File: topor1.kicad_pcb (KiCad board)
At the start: 2 copper layers, 99.8 x 99.8 mm, 76 parts, among them IC1 ATMEGA168-A, P1 CONN_01X02_PWR, P2 USB_B, P3 CONN_02X13_X0, P4 CONN_02X13_X3, P5 CONN_02X13_X1, P6 CONN_02X07_JTAG, U1 AP1117_ADJ, U2 AP1117_33, U3 AP1117_ADJ, U4 FT232RL, U5 M25P16-VME, U6 ECS-3963, U7 XC6SLX9-TQG144, Y1 11.059MHz

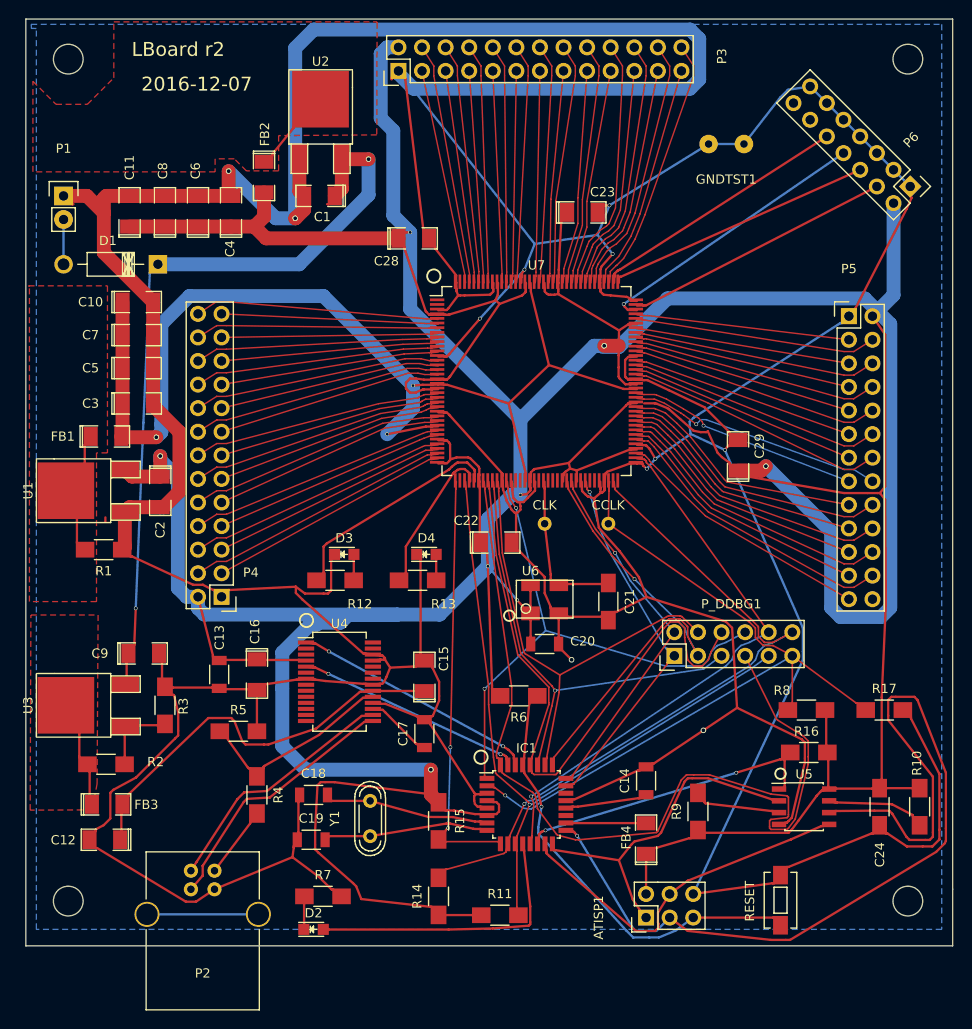
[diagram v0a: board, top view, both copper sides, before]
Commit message: Spartan-6 chip position was changed to avoid problems with a bent tracks. CD6 net was rerouted.
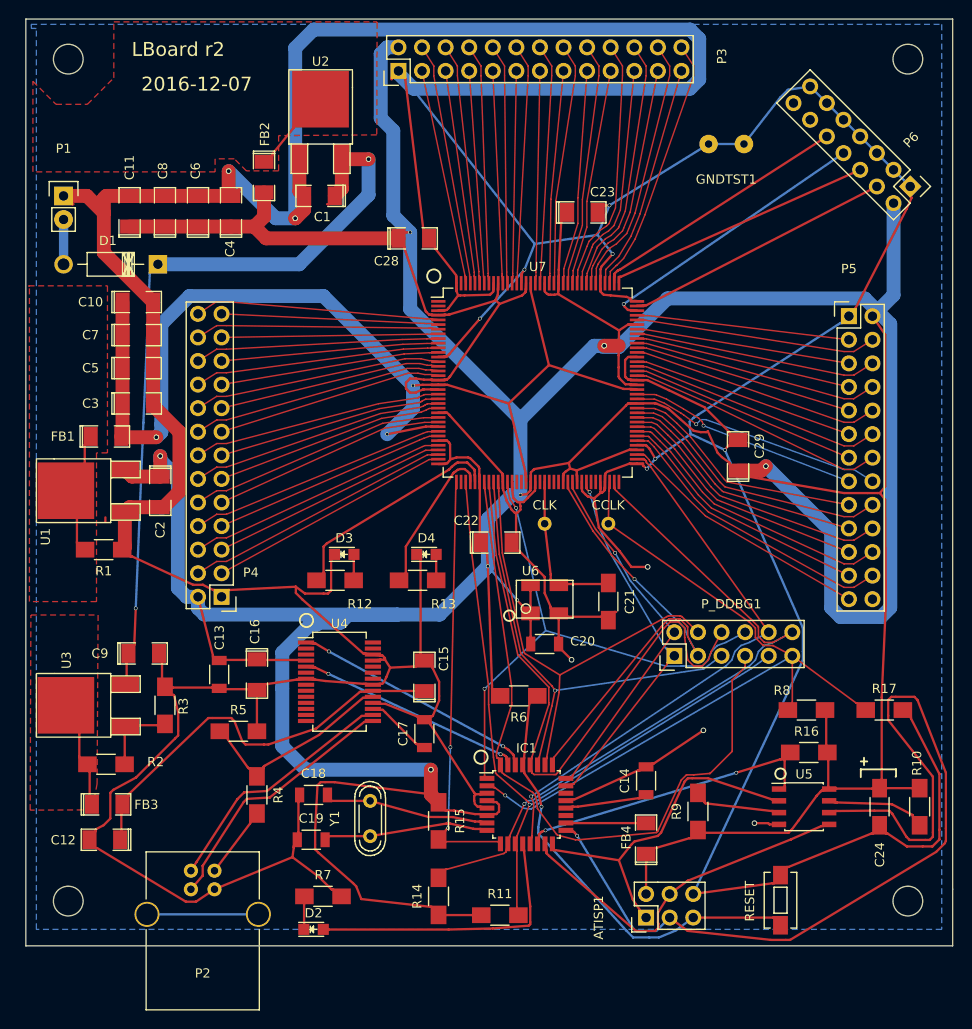
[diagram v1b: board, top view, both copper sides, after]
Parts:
- moved U7 0.21 mm to (120.2, 102.2)
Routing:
- net GND: track 836.7 -> 793.6 mm, vias 11 -> 13
- net /mcu/CD6: track 99.3 -> 76.0 mm

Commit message: bumped revision number, made some minort track layout changes
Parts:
- moved U7 0.05 mm to (120.2, 102.1)
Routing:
- net GND: track 793.6 -> 794.8 mm
- net /mcu/CD0: track 39.8 -> 40.6 mm
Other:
- board text added: "2016-12-20"
- board text added: "LBoard r3"
- board text removed: "2016-12-07"
- board text removed: "LBoard r2"

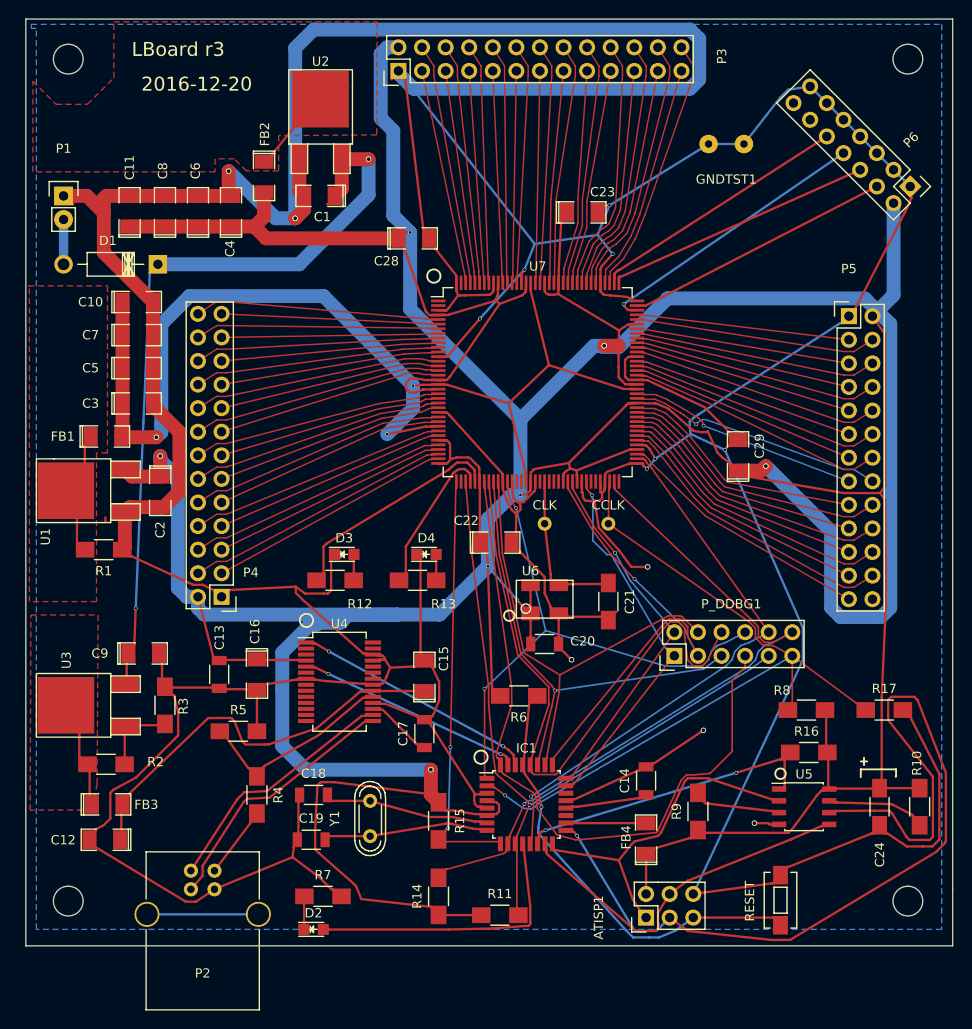
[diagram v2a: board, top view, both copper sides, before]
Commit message: footprint of oscillator Y1 changed. Some silscreen changes
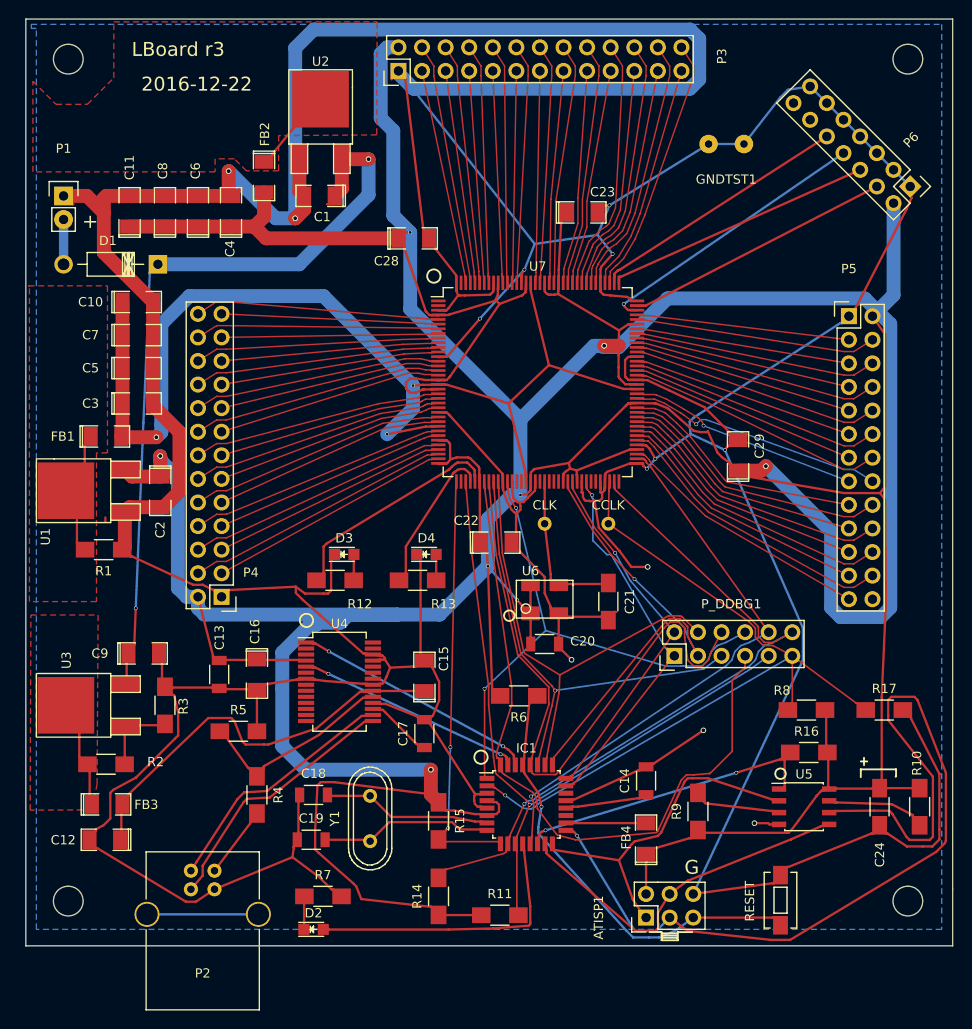
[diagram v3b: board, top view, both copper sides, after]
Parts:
- Y1: footprint Crystals:Crystal_HC52-U_Vertical -> Crystals:Crystal_HC49-U_Vertical
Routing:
- net Net-(C19-Pad2): track 17.8 -> 20.2 mm
- net Net-(C18-Pad2): track 17.8 -> 19.1 mm
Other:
- board text added: "+"
- board text added: "2016-12-22"
- board text added: "G"
- board text removed: "2016-12-20"

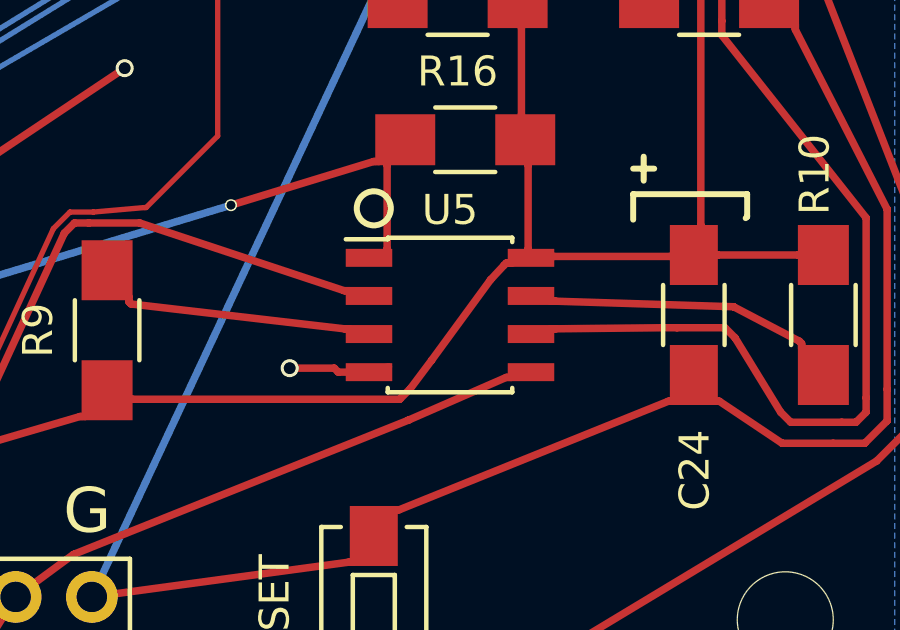
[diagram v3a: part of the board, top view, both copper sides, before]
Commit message: New footprint for SOIC-8W.
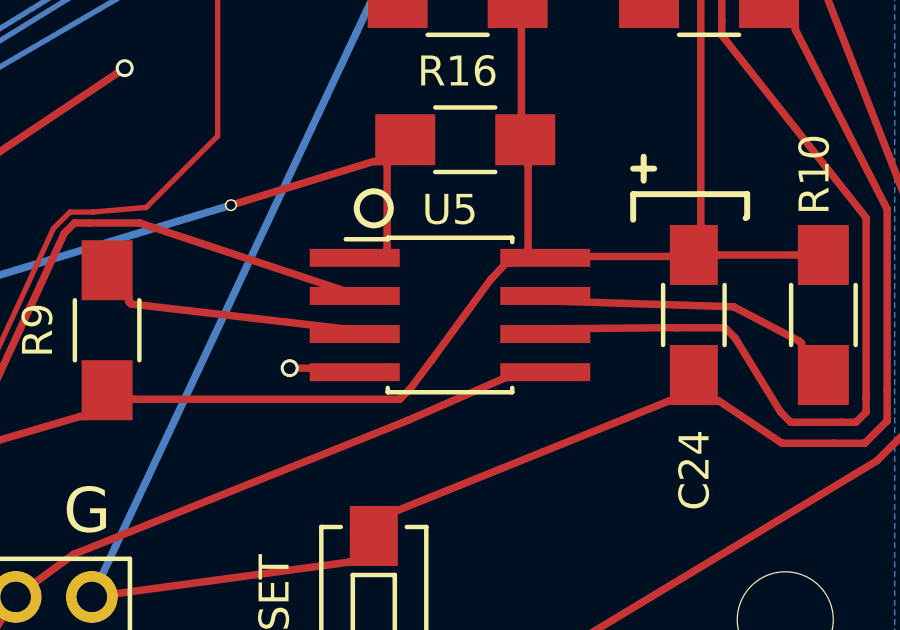
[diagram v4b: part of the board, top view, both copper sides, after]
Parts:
- U5: footprint Housings_SOIC:SOIC-8_3.9x4.9mm_Pitch1.27mm -> SOIC-8W-LONGPAD:SOIC-8_5.49x5.49mm_Pitch1.27mm
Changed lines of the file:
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@@
-    )
-  )
-  (module Housings_SOIC:SOIC-8_3.9x4.9mm_Pitch1.27mm (layer F.Cu)
-    (at 148.844 147.828)
-    (descr "8-Lead Plastic Small Outline (SN) - Narrow, 3.90 mm Body [SOIC] (see Microchip Packaging Specification 00000049BS.pdf)")
-    (tags "SOIC 1.27")
-    (attr smd)
-    (fp_text reference U5 (at 0 -3.5) (layer F.SilkS)
-      (effects (font (size 1 1) (thickness 0.15)))
-    )
-    (fp_text value M25P16-VME (at 0 3.5) (layer F.Fab)
-      (effects (font (size 1 1) (thickness 0.15)))
-    )
-    (fp_line (start -0.95 -2.45) (end 1.95 -2.45) (layer F.Fab) (width 0.15))
-    (fp_line (start 1.95 -2.45) (end 1.95 2.45) (layer F.Fab) (width 0.15))
-    (fp_line (start 1.95 2.45) (end -1.95 2.45) (layer F.Fab) (width 0.15))
-    (fp_line (start -1.95 2.45) (end -1.95 -1.45) (layer F.Fab) (width 0.15))
-    (fp_line (start -1.95 -1.45) (end -0.95 -2.45) (layer F.Fab) (width 0.15))
-    (fp_line (start -3.75 -2.75) (end -3.75 2.75) (layer F.CrtYd) (width 0.05))
-    (fp_line (start 3.75 -2.75) (end 3.75 2.75) (layer F.CrtYd) (width 0.05))
-    (fp_line (start -3.75 -2.75) (end 3.75 -2.75) (layer F.CrtYd) (width 0.05))
-    (fp_line (start -3.75 2.75) (end 3.75 2.75) (layer F.CrtYd) (width 0.05))
-    (fp_line (start -2.075 -2.575) (end -2.075 -2.525) (layer F.SilkS) (width 0.15))
-    (fp_line (start 2.075 -2.575) (end 2.075 -2.43) (layer F.SilkS) (width 0.15))
-    (fp_line (start 2.075 2.575) (end 2.075 2.43) (layer F.SilkS) (width 0.15))
-    (fp_line (start -2.075 2.575) (end -2.075 2.43) (layer F.SilkS) (width 0.15))
-    (fp_line (start -2.075 -2.575) (end 2.075 -2.575) (layer F.SilkS) (width 0.15))
-    (fp_line (start -2.075 2.575) (end 2.075 2.575) (layer F.SilkS) (width 0.15))
-    (fp_line (start -2.075 -2.525) (end -3.475 -2.525) (layer F.SilkS) (width 0.15))
-    (pad 1 smd rect (at -2.7 -1.905) (size 1.55 0.6) (layers F.Cu F.Paste F.Mask)
-      (net 30 "Net-(IC1-Pad14)"))
-    (pad 2 smd rect (at -2.7 -0.635) (size 1.55 0.6) (layers F.Cu F.Paste F.Mask)
-      (net 1 /mcu/MISO))
-    (pad 3 smd rect (at -2.7 0.635) (size 1.55 0.6) (layers F.Cu F.Paste F.Mask)
-      (net 126 "Net-(R9-Pad2)"))
-    (pad 4 smd rect (at -2.7 1.905) (size 1.55 0.6) (layers F.Cu F.Paste F.Mask)
-      (net 6 GND))
-    (pad 5 smd rect (at 2.7 1.905) (size 1.55 0.6) (layers F.Cu F.Paste F.Mask)
-      (net 4 /mcu/MOSI))
-    (pad 6 smd rect (at 2.7 0.635) (size 1.55 0.6) (layers F.Cu F.Paste F.Mask)
-      (net 3 "Net-(ATISP1-Pad3)"))
-    (pad 7 smd rect (at 2.7 -0.635) (size 1.55 0.6) (layers F.Cu F.Paste F.Mask)
-      (net 127 "Net-(R10-Pad2)"))
-    (pad 8 smd rect (at 2.7 -1.905) (size 1.55 0.6) (layers F.Cu F.Paste F.Mask)
-      (net 2 +3V3))
-    (model Housings_SOIC.3dshapes/SOIC-8_3.9x4.9mm_Pitch1.27mm.wrl
-      (at (xyz 0 0 0))
-      (scale (xyz 1 1 1))
-      (rotate (xyz 0 0 0))
     )
   )
@@
       (net 12 "Net-(C18-Pad2)"))
   )
+  (module SOIC-8W-LONGPAD:SOIC-8_5.49x5.49mm_Pitch1.27mm (layer F.Cu)
+    (at 148.844 147.828)
+    (tags "SOIC 1.27")
+    (attr smd)
+    (fp_text reference U5 (at 0 -3.5) (layer F.SilkS)
+      (effects (font (size 1 1) (thickness 0.15)))
+    )
+    (fp_text value M25P16-VME (at 0 3.5) (layer F.Fab)
+      (effects (font (size 1 1) (thickness 0.15)))
+    )
+    (fp_line (start -0.95 -2.45) (end 1.95 -2.45) (layer F.Fab) (width 0.15))
+    (fp_line (start 1.95 -2.45) (end 1.95 2.45) (layer F.Fab) (width 0.15))
+    (fp_line (start 1.95 2.45) (end -1.95 2.45) (layer F.Fab) (width 0.15))
+    (fp_line (start -1.95 2.45) (end -1.95 -1.45) (layer F.Fab) (width 0.15))
+    (fp_line (start -1.95 -1.45) (end -0.95 -2.45) (layer F.Fab) (width 0.15))
+    (fp_line (start -4.953 -2.7305) (end -4.953 2.7695) (layer F.CrtYd) (width 0.05))
+    (fp_line (start 4.953 -2.7305) (end 4.953 2.7695) (layer F.CrtYd) (width 0.05))
+    (fp_line (start -4.953 -2.7305) (end 4.953 -2.7305) (layer F.CrtYd) (width 0.05))
+    (fp_line (start -4.953 2.794) (end 4.953 2.794) (layer F.CrtYd) (width 0.05))
+    (fp_line (start -2.075 -2.575) (end -2.075 -2.525) (layer F.SilkS) (width 0.15))
+    (fp_line (start 2.075 -2.575) (end 2.075 -2.43) (layer F.SilkS) (width 0.15))
+    (fp_line (start 2.075 2.575) (end 2.075 2.43) (layer F.SilkS) (width 0.15))
+    (fp_line (start -2.075 2.575) (end -2.075 2.43) (layer F.SilkS) (width 0.15))
+    (fp_line (start -2.075 -2.575) (end 2.075 -2.575) (layer F.SilkS) (width 0.15))
+    (fp_line (start -2.075 2.575) (end 2.075 2.575) (layer F.SilkS) (width 0.15))
+    (fp_line (start -2.075 -2.525) (end -3.475 -2.525) (layer F.SilkS) (width 0.15))
+    (pad 1 smd rect (at -3.175 -1.905) (size 3 0.6) (layers F.Cu F.Paste F.Mask)
+      (net 30 "Net-(IC1-Pad14)"))
+    (pad 2 smd rect (at -3.175 -0.635) (size 3 0.6) (layers F.Cu F.Paste F.Mask)
+      (net 1 /mcu/MISO))
+    (pad 3 smd rect (at -3.175 0.635) (size 3 0.6) (layers F.Cu F.Paste F.Mask)
+      (net 126 "Net-(R9-Pad2)"))
+    (pad 4 smd rect (at -3.175 1.905) (size 3 0.6) (layers F.Cu F.Paste F.Mask)
+      (net 6 GND))
+    (pad 5 smd rect (at 3.175 1.905) (size 3 0.6) (layers F.Cu F.Paste F.Mask)
+      (net 4 /mcu/MOSI))
+    (pad 6 smd rect (at 3.175 0.635) (size 3 0.6) (layers F.Cu F.Paste F.Mask)
+      (net 3 "Net-(ATISP1-Pad3)"))
+    (pad 7 smd rect (at 3.175 -0.635) (size 3 0.6) (layers F.Cu F.Paste F.Mask)
+      (net 127 "Net-(R10-Pad2)"))
+    (pad 8 smd rect (at 3.175 -1.905) (size 3 0.6) (layers F.Cu F.Paste F.Mask)
+      (net 2 +3V3))
+  )
   (gr_text + (at 71.96 84.78) (layer F.SilkS)

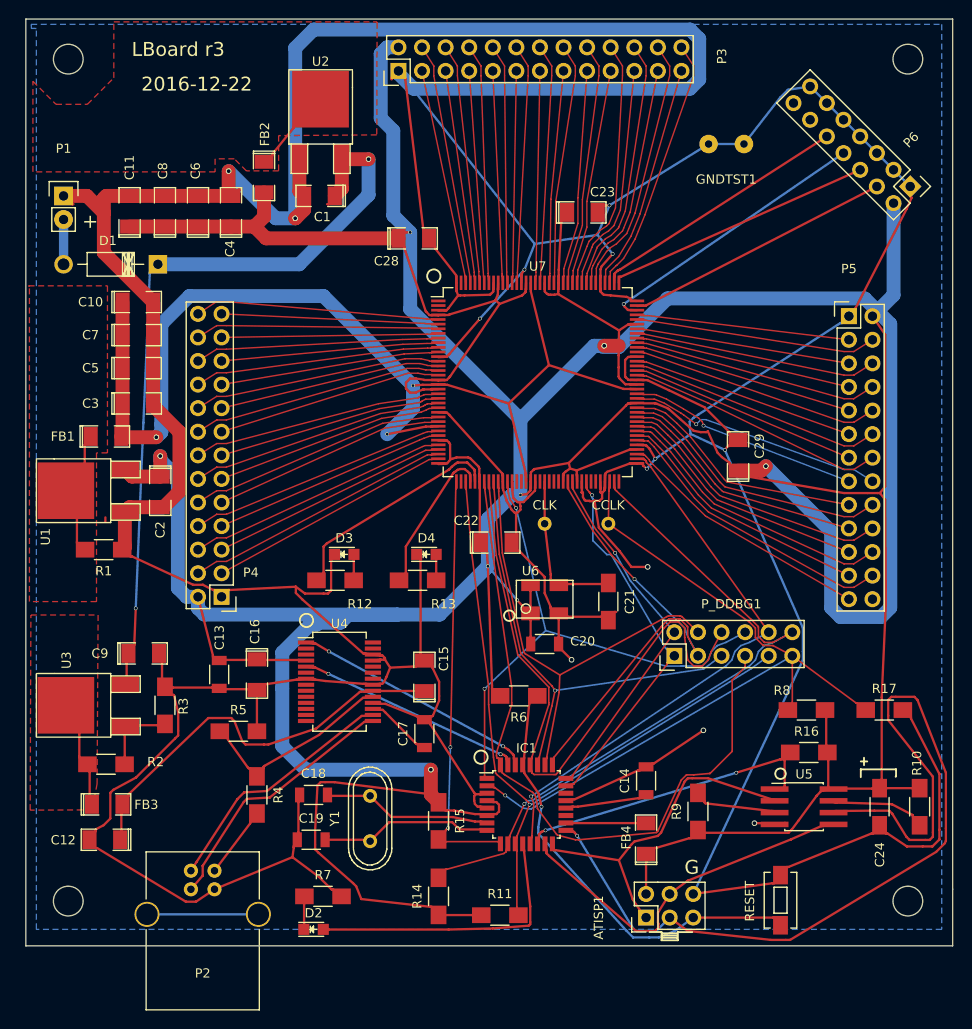
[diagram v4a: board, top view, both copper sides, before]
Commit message: Silkscreen changes
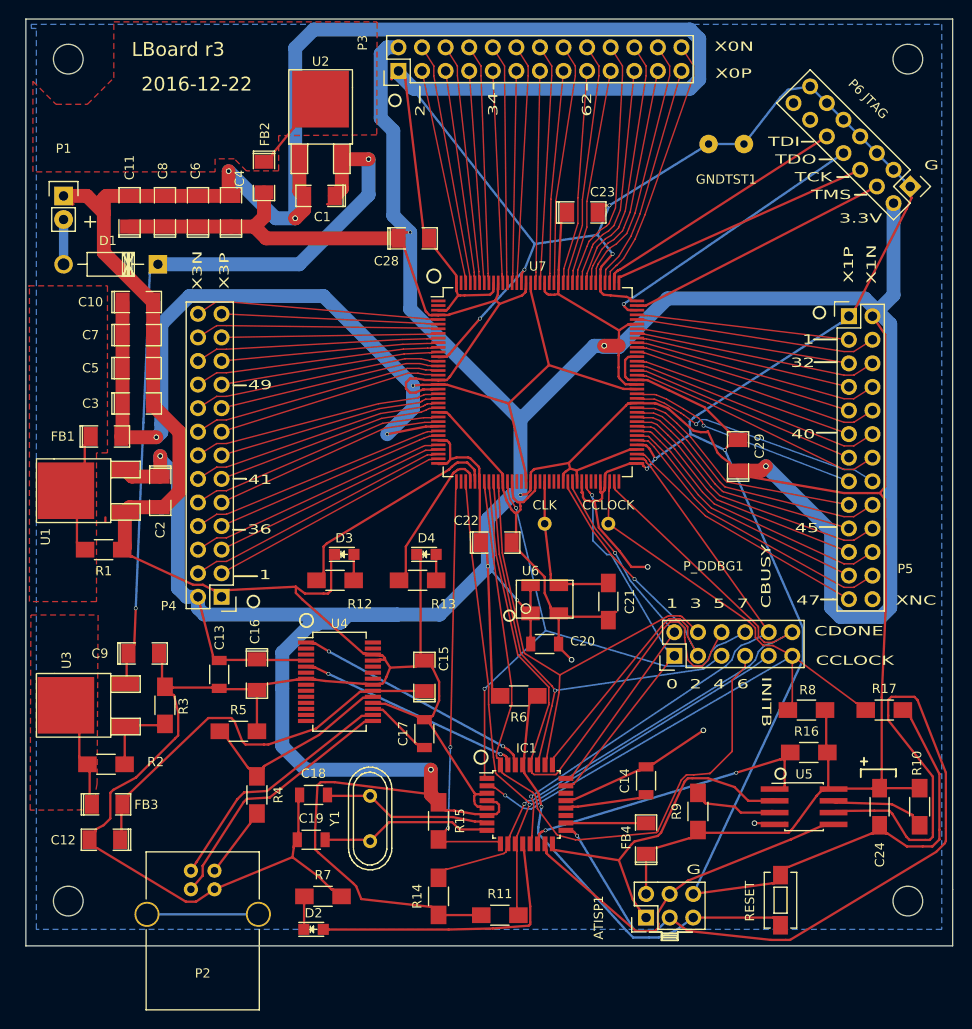
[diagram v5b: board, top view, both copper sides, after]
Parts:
- P6 JTAG: renamed from P6
- renumbered CCLK to CCLOCK
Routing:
- net /mcu/MISO: track 37.2 -> 38.0 mm
- net Net-(R9-Pad2): track 9.42 -> 10.0 mm
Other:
- board text added: "0"
- board text added: "1"
- board text added: "2"
- board text added: "3"
- board text added: "3.3V"
- board text added: "32"
- board text added: "34"
- board text added: "36"
- board text added: "4"
- board text added: "40"
- board text added: "41"
- board text added: "45"
- board text added: "47"
- board text added: "49"
- board text added: "5"
- board text added: "6"
- board text added: "62"
- board text added: "7"
- board text added: "CBUSY"
- board text added: "CCLOCK"
- board text added: "CDONE"
- board text added: "INITB"
- board text added: "TCK"
- board text added: "TDI"
- board text added: "TDO"
- board text added: "TMS"
- board text added: "X0N"
- board text added: "X0P"
- board text added: "X1N"
- board text added: "X1P"
- board text added: "X3N"
- board text added: "X3P"
- board text added: "XNC"
